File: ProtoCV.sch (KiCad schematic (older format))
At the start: 142 parts, among them J1 AudioJack2_SwitchT, J10 Conn_01x01_Male, J11 Conn_01x05_Male, J12 Conn_01x09_Male, J13 AudioJack2_SwitchT, J14 AudioJack2_SwitchT, J15 AudioJack2_SwitchT, J16 AudioJack2_SwitchT, J17 AudioJack2_SwitchT, J18 AudioJack2_SwitchT, J19 AudioJack2_SwitchT, J2 AudioJack2_SwitchT, J20 AudioJack2_SwitchT, J21 Conn_01x01_Male, J22 Conn_01x01_Male, J23 Conn_01x01_Male, J24 Conn_01x01_Male, J25 Conn_01x01_Male, J26 Conn_01x01_Male, J27 Conn_01x01_Male, J28 Conn_01x01_Male, J29 Conn_01x01_Male, J3 AudioJack2_SwitchT, J30 Conn_01x01_Male, J4 AudioJack2_SwitchT, J5 AudioJack2_SwitchT, J6 AudioJack2_SwitchT, J7 AudioJack2_SwitchT, J8 AudioJack2_SwitchT, J9 Conn_02x05_Odd_Even, Q1 BC847, Q2 BC847, Q3 BC847, Q4 BC847, Q5 BC847, Q6 BC847, Q7 BC847, Q8 BC847, U1 OPA4192, U2 OPA4192, U3 ADC80508Z, U4 R-78E3.3-0.5, U5 LD2981ABU33TR, U6 74AHCT244, U7 L7805

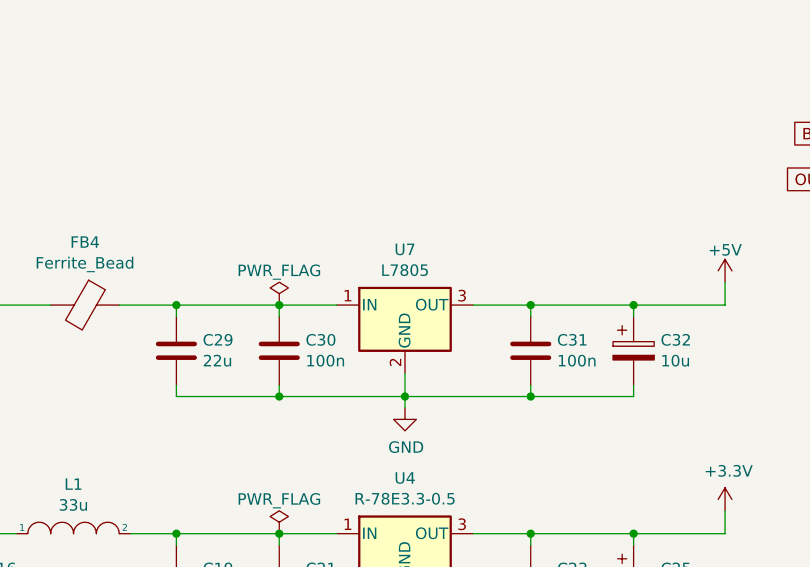
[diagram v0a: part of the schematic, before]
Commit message: Corrected footprint for 5V regulator.
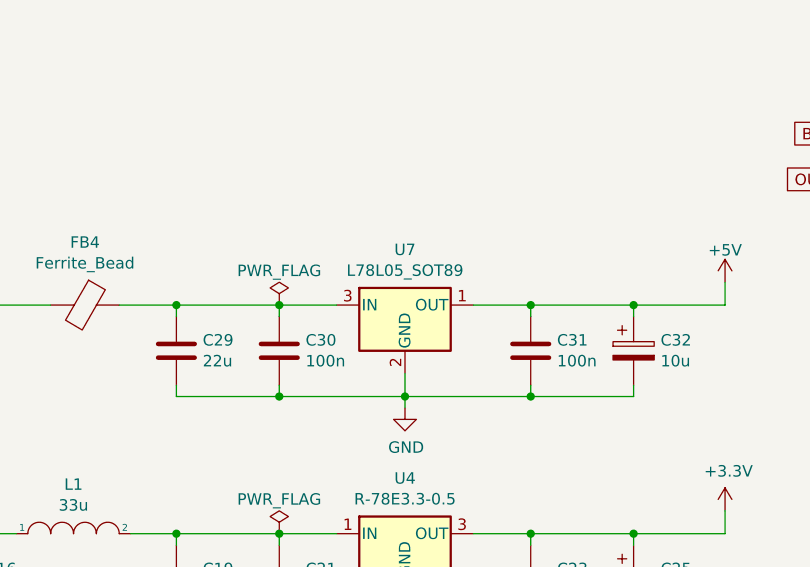
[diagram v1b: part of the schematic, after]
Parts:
- removed U7: L7805, Package_TO_SOT_SMD:SOT-223-3_TabPin2, symbol Regulator_Linear:L7805
- added U7: L78L05_SOT89, Package_TO_SOT_SMD:SOT-89-3, symbol Local:L78L05_SOT89
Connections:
- net +5V: now also U7.1 (OUT)
- net GND: now also U7.2 (GND)
- net at C29.1, C30.1, FB4.1: now also U7.3 (IN)
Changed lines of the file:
@@
 	6750 6550 6750 6450
-$Comp
-L Regulator_Linear:L7805 U?
-U 1 1 5F630377
-P 5350 6550
-AR Path="/5F606346/5F630377" Ref="U?"  Part="1"
-AR Path="/5F630377" Ref="U7"  Part="1"
-F 0 "U7" H 5350 6792 50  0000 C CNN
-F 1 "L7805" H 5350 6701 50  0000 C CNN
-F 2 "Package_TO_SOT_SMD:SOT-223-3_TabPin2" H 5375 6400 50  0001 L CIN
-F 3 "http://www.st.com/content/ccc/resource/technical/document/datasheet/41/4f/b3/b0/12/d4/47/88/CD00000444.pdf/files/CD00000444.pdf/jcr:content/translations/en.CD00000444.pdf" H 5350 6500 50  0001 C CNN
-	1    5350 6550
-	1    0    0    -1
-$EndComp
 $Comp
 L Device:C C?
@@
 Text GLabel 3600 2150 2    50   Input ~ 0
 OUT4
+$Comp
+L Local:L78L05_SOT89 U7
+U 1 1 5FCEF2AA
+P 5350 6550
+F 0 "U7" H 5350 6792 50  0000 C CNN
+F 1 "L78L05_SOT89" H 5350 6701 50  0000 C CNN
+F 2 "Package_TO_SOT_SMD:SOT-89-3" H 5350 6750 50  0001 C CIN
+F 3 "http://www.st.com/content/ccc/resource/technical/document/datasheet/15/55/e5/aa/23/5b/43/fd/CD00000446.pdf/files/CD00000446.pdf/jcr:content/translations/en.CD00000446.pdf" H 5350 6500 50  0001 C CNN
+	1    5350 6550
+	1    0    0    -1
+$EndComp
 $EndSCHEMATC
